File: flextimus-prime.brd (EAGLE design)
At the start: 78.7 x 65.7 mm, 41 parts, among them T1 2N2222, U1 STM32F042KXU, U2 IP4220CZ6, U3 MCP1802T-3302I/OT

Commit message: better board, for real
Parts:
- removed CN1: (no value), adafruit:USB-MINIB-THM-MOLEX
- removed U2: IP4220CZ6, IP4220CZ6:SOT457
- added CN2: (no value), adafruit:USB-MINIB
- moved TP8 18.1 mm to (30.5, 6.12)
- moved R6 17.3 mm to (59.7, 12.1)
- moved R3 15.3 mm to (63.1, 11.3), turned to 270 degrees
- moved R4 13.1 mm to (65.1, 15.9)
- moved TP6 11.6 mm to (33.9, 6.10)
- moved FB1 10.3 mm to (52.9, 10.0), turned to 180 degrees
- moved R10 10.1 mm to (52.0, 32.0)
- moved TP5 9.67 mm to (26.7, 6.22)
- moved R7 9.33 mm to (31.0, 30.8), turned to 270 degrees
- moved R5 9.06 mm to (43.0, 6.30)
- moved C8 8.01 mm to (52.8, 13.6)
- moved R1 3.23 mm to (26.7, 10.6)
- moved R9 2.97 mm to (48.2, 23.3)
- moved C7 2.68 mm to (55.0, 13.6)
- moved C1 2.22 mm to (34.2, 28.4), turned to 180 degrees
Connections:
- removed net USBM: CN1.D+, U2.6
- removed net USBP: CN1.D-, U2.1
- net GND: now also CN2.GND; no longer CN1.GND, U2.2
- net VBUS: now also CN2.VBUS; no longer CN1.VBUS, U2.5
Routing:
- net 3.3V: track 0.00 -> 291.2 mm, vias 0 -> 15
- net BUT2: track 0.00 -> 70.9 mm, vias 0 -> 2
- net N$3: track 0.00 -> 68.0 mm, vias 0 -> 2
- net BUT1: track 0.00 -> 61.6 mm, vias 0 -> 4
- net N$21: track 0.00 -> 58.5 mm, vias 0 -> 2
- net NRST: track 0.00 -> 50.5 mm, vias 0 -> 2
- net N$10: track 0.00 -> 47.0 mm
- net SWDIO: track 0.00 -> 45.7 mm
- net N$1: track 0.00 -> 44.8 mm, vias 0 -> 3
- net N$11: track 0.00 -> 44.6 mm
- net N$7: track 0.00 -> 44.3 mm, vias 0 -> 1
- net SWCLK: track 0.00 -> 42.3 mm
- net N$12: track 0.00 -> 42.1 mm
- net N$13: track 0.00 -> 39.7 mm
- net AVDD: track 0.00 -> 39.5 mm, vias 0 -> 2
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- added copper zone on layer 16, net GND
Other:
- board text added: "ECE411 Fall 2017 Team 7 Board Rev 1.1"

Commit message: schematic + board rev 1.2
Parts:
- added C2: 100n, rcl:C0805
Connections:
- net 3.3V: now also C2.1
- net GND: now also C2.2
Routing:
- net 3.3V: track 291.2 -> 294.5 mm
- net N$10: track 47.0 -> 43.8 mm
- net N$12: track 42.1 -> 40.2 mm
- net N$11: track 44.6 -> 42.8 mm
- net N$13: track 39.7 -> 38.6 mm
- net N$14: track 37.2 -> 37.8 mm
- net N$3: track 68.0 -> 68.6 mm
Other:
- board text added: "ECE411 Fall 2017 Team 7 Board Rev 1.2"
- board text removed: "ECE411 Fall 2017 Team 7 Board Rev 1.1"

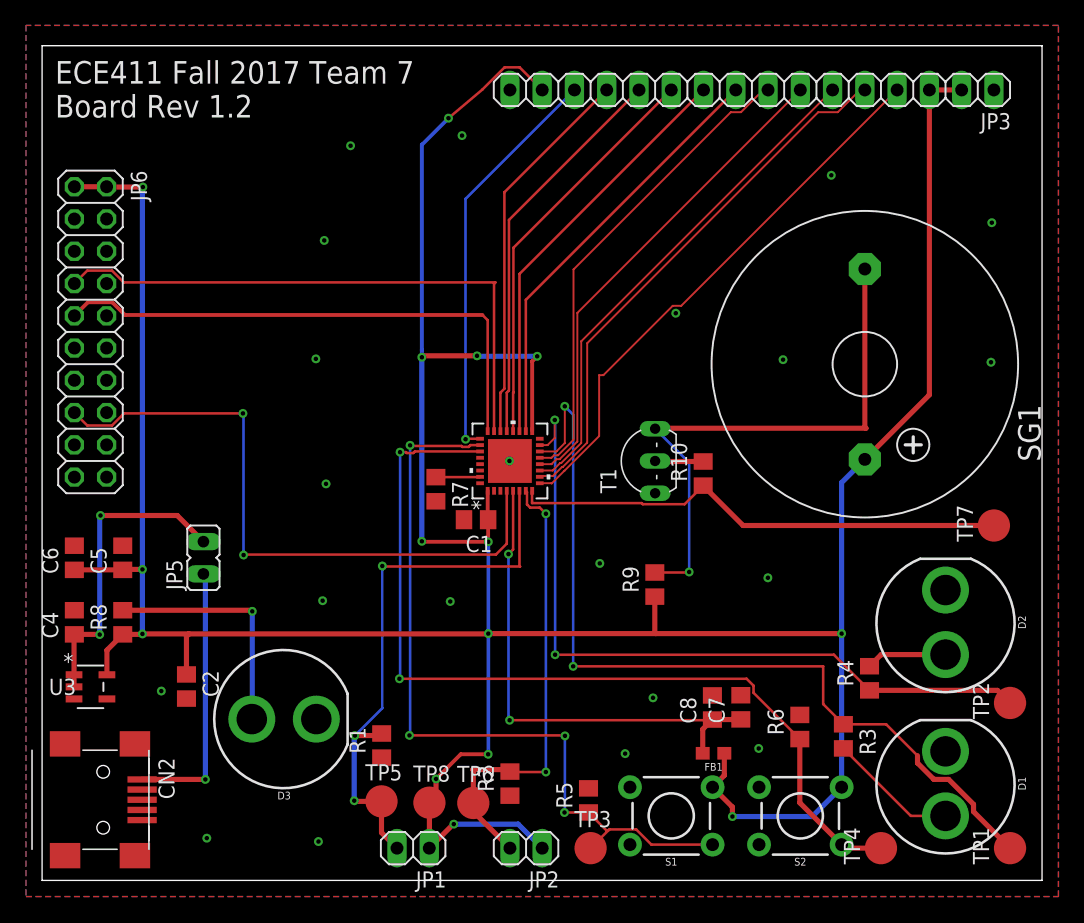
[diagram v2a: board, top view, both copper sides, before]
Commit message: minor tweaks to board rev 1.2
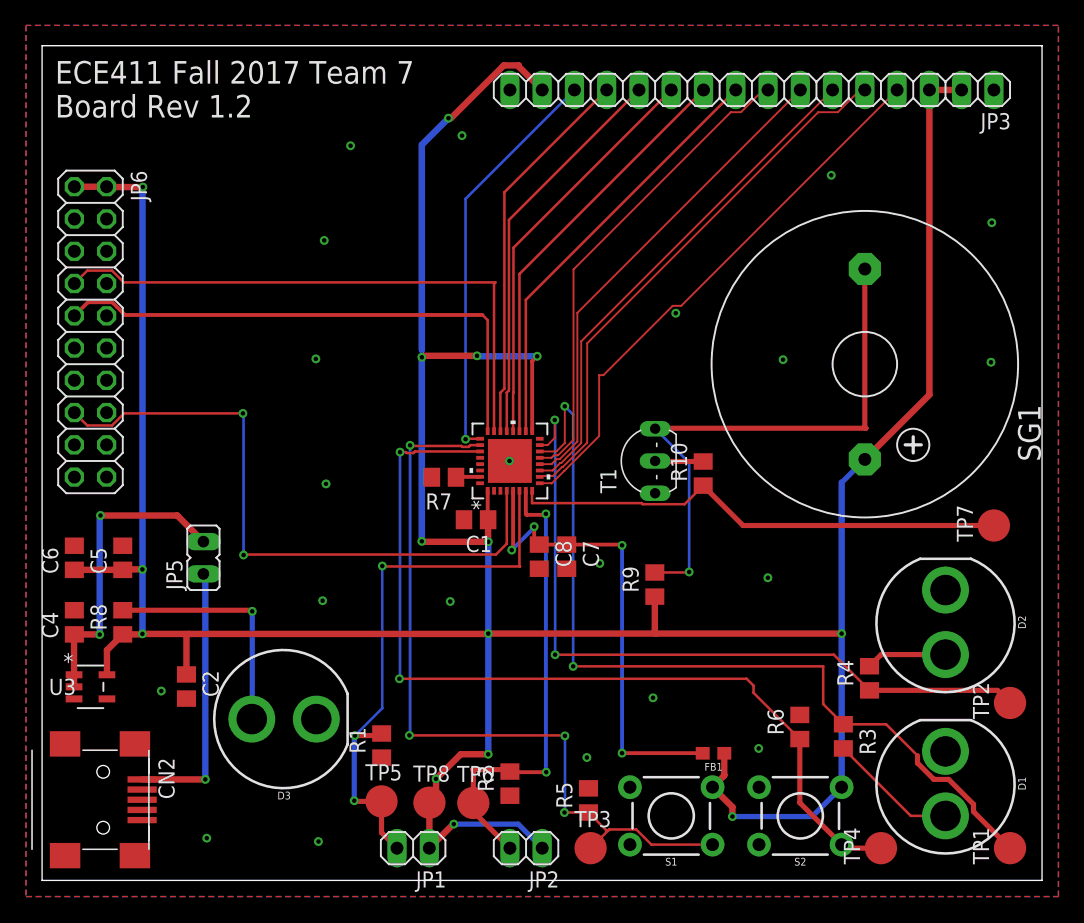
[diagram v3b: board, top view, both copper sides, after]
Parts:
- moved C7 18.1 mm to (41.3, 25.5), turned to 270 degrees
- moved C8 18.1 mm to (39.1, 25.5), turned to 270 degrees
- moved R7 1.13 mm to (31.6, 31.7), turned to 180 degrees
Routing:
- net N$20: track 3.49 -> 1.94 mm
- net AVDD: track 39.5 -> 38.1 mm, vias 2 -> 4
- net N$2: track 36.5 -> 37.1 mm

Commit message: Auto stash before merge of "master" and "origin/master"
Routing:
- net 3.3V: track 294.8 -> 295.8 mm

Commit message: minor trace tweak
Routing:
- net 3.3V: track 295.8 -> 295.1 mm
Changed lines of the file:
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@@
 <wire x1="11.3665" y1="19.2151" x2="11.557" y2="19.4056" width="0.4064" layer="1"/>
 <wire x1="38.580440625" y1="35.37" x2="38.580440625" y2="40.866440625" width="0.3048" layer="1"/>
-<wire x1="36.34603125" y1="64.1604" x2="37.5285" y2="64.1604" width="0.508" layer="1"/>
-<wire x1="31.9913" y1="60.0075" x2="32.19313125" y2="60.0075" width="0.508" layer="1"/>
-<wire x1="32.19313125" y1="60.0075" x2="36.34603125" y2="64.1604" width="0.508" layer="1"/>
-<wire x1="37.5285" y1="64.1604" x2="37.5285" y2="64.0715" width="0.508" layer="1"/>
-<wire x1="37.5285" y1="64.0715" x2="39.37" y2="62.23" width="0.508" layer="1"/>
+<wire x1="32.19313125" y1="60.0075" x2="31.9913" y2="60.0075" width="0.508" layer="1"/>
+<wire x1="31.9913" y1="60.0075" x2="38.4683" y2="60.0075" width="0.8128" layer="1"/>
+<wire x1="39.37" y1="60.9092" x2="39.37" y2="62.23" width="0.8128" layer="1"/>
+<wire x1="38.4683" y1="60.0075" x2="39.37" y2="60.9092" width="0.8128" layer="1"/>
 </signal>
 <signal name="GND">
